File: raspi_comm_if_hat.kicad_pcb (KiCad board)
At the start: 2 copper layers, 65 x 56 mm, 64 parts, among them J1 B04B-XA, J2 Conn_02x20_Odd_Even, J3 B04B-XA, J4 Conn_01x02, J5 Conn_01x04, J6 B04B-XA, Q1 Q_NMOS_GSD, Q2 Q_NMOS_GSD, Q3 Q_NMOS_GSD, Q4 Q_NMOS_GSD, Q5 Q_NMOS_GSD, SW1 SW_DIP_x01, SW2 SW_DIP_x02, U1 MCP25625-x-SS, U2 74AHC1G04, U3 74AHC1G04, U4 TCK106AF, U5 TCK106AF, U6 CH213K, U7 CH213K, U8 TCK106AF, U9 TCK106AF, Y1 20MHz

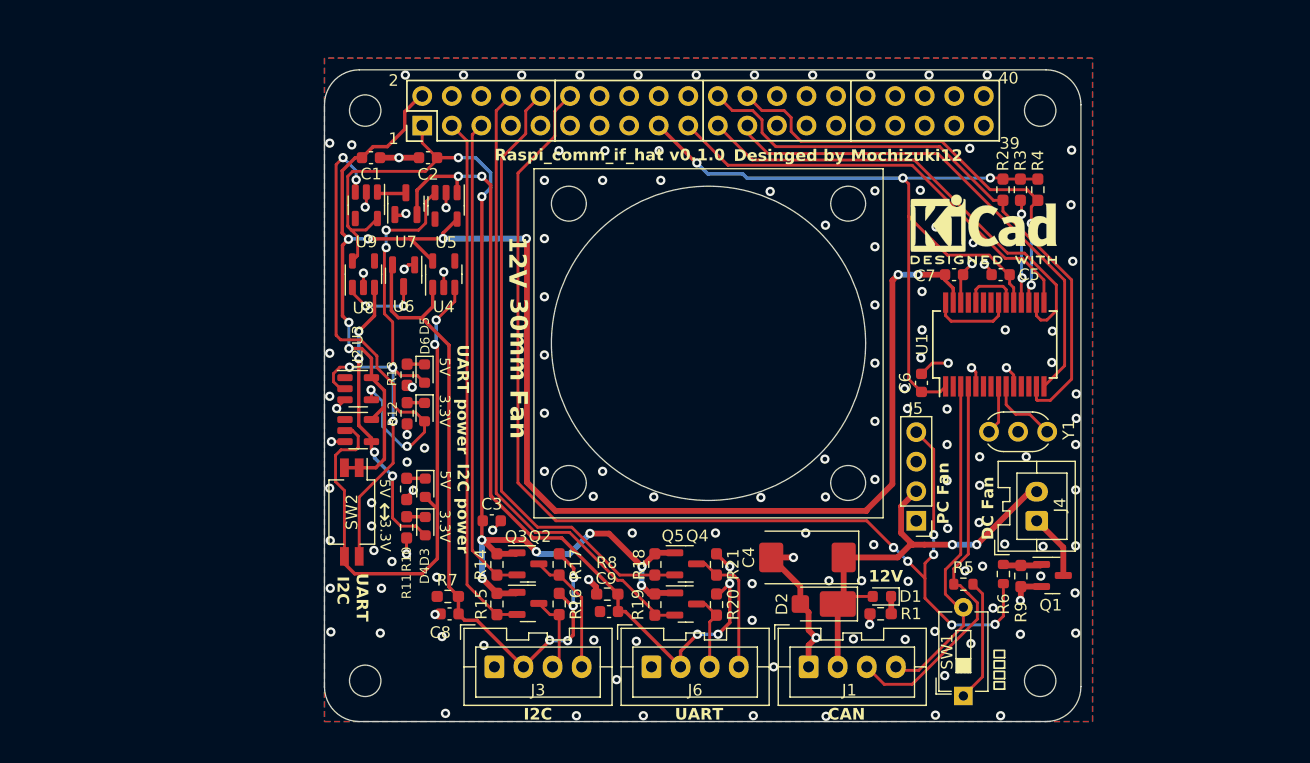
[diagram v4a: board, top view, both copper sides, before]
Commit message: Update of data for PCBA
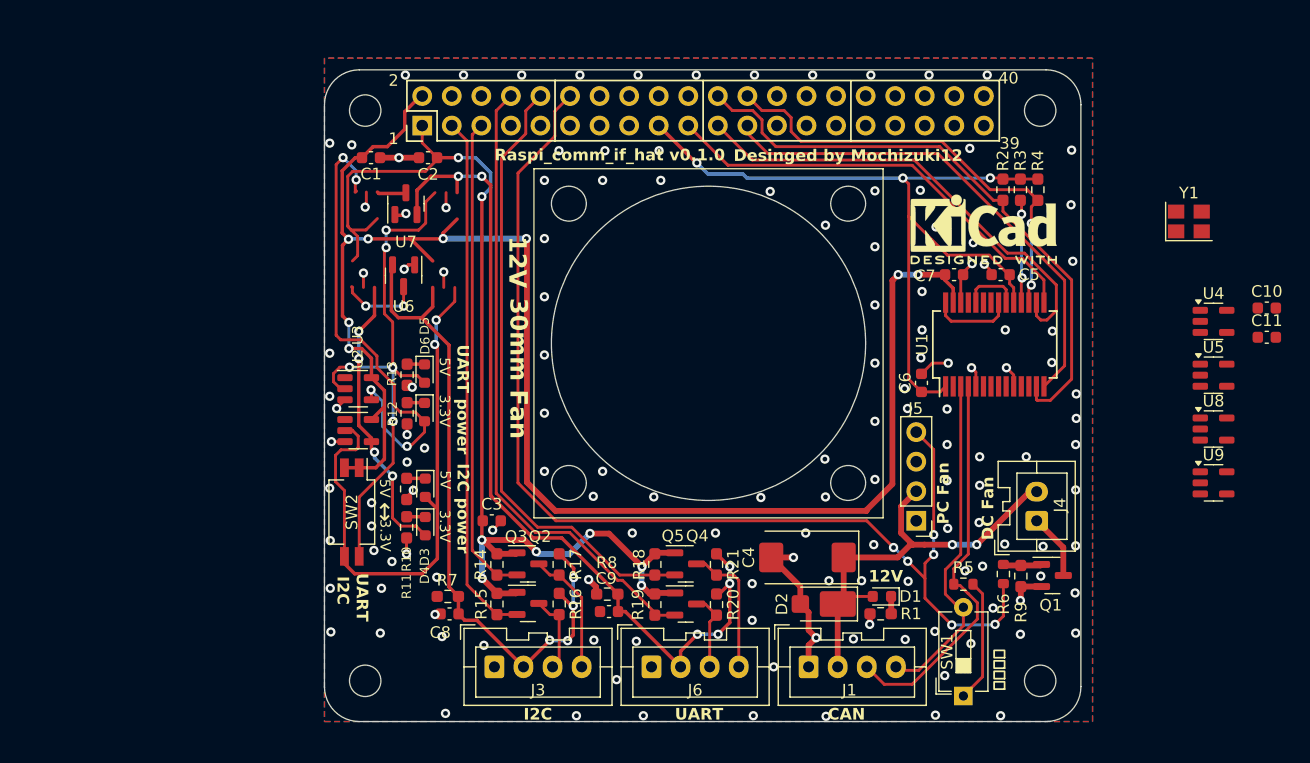
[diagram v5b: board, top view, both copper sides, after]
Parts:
- added C10: 9pF, Capacitor_SMD:C_0603_1608Metric, F.Cu at (181.0, 74.5)
- added C11: 9pF, Capacitor_SMD:C_0603_1608Metric, F.Cu at (181.0, 77.0)
- U4, U5, U8, U9: value TCK106AF -> AP2171W
- U6, U7: value CH213K -> AP2331
- Y1: value 20MHz -> 16MHz; footprint Crystal:Resonator_Murata_CSTLSxxxX-3Pin_W5.5mm_H3.0mm -> Crystal:Crystal_SMD_3225-4Pin_3.2x2.5mm
- moved U9 76.6 mm to (176.4, 89.5), turned to 0 degrees
- moved U8 74.2 mm to (176.4, 84.9), turned to 0 degrees
- moved U5 67.5 mm to (176.4, 80.2), turned to 0 degrees
- moved U4 66.3 mm to (176.4, 75.6), turned to 0 degrees
- moved Y1 21.8 mm to (174.3, 67.0), turned to 0 degrees
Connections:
- U4 pad 3: Net-(D3-A) -> unconnected-(U4-~{FLG}-Pad3)
- U4 pad 4: unconnected-(U4-NC-Pad4) -> Net-(D3-A)
- U5 pad 3: Net-(D5-A) -> unconnected-(U5-~{FLG}-Pad3)
- U5 pad 4: unconnected-(U5-NC-Pad4) -> Net-(D5-A)
- U8 pad 3: Net-(D4-A) -> unconnected-(U8-~{FLG}-Pad3)
- U8 pad 4: unconnected-(U8-NC-Pad4) -> Net-(D3-A)
- U9 pad 3: Net-(D6-A) -> unconnected-(U9-~{FLG}-Pad3)
- U9 pad 4: unconnected-(U9-NC-Pad4) -> Net-(D5-A)
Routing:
- net Net-(U1-OSC1): track 6.06 -> 0.00 mm
- net Net-(U1-OSC2): track 4.24 -> 0.00 mm

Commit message: Add LSCS
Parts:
- removed SW1: SW_DIP_x01, Button_Switch_THT:SW_DIP_SPSTx01_Slide_6.7x4.1mm_W7.62mm_P2.54mm_LowProfile
- added JP1: Jumper_2_Open, Connector_PinHeader_2.54mm:PinHeader_1x02_P2.54mm_Vertical, F.Cu at (154.7, 107.4)
- C10, C11: value 9pF -> 10pF; footprint Capacitor_SMD:C_0603_1608Metric -> Capacitor_SMD:C_0402_1005Metric
- C3, C5, C6, C7, C8, C9: footprint Capacitor_SMD:C_0603_1608Metric -> Capacitor_SMD:C_0402_1005Metric
- C4: value 100uF -> 10uF; footprint Capacitor_Tantalum_SMD:CP_EIA-7343-15_Kemet-W -> Capacitor_SMD:C_0603_1608Metric
- D2: footprint Diode_SMD:Vishay_SMPA -> Diode_SMD:D_SOD-123F
- R1, R10, R11, R12, R13, R14, R15, R16, R17, R18, R19, R2, R20, R21, R3, R4, R7, R8, R9: footprint Resistor_SMD:R_0603_1608Metric_Pad0.98x0.95mm_HandSolder -> Resistor_SMD:R_0402_1005Metric
- R6: footprint Resistor_SMD:R_0603_1608Metric -> Resistor_SMD:R_0402_1005Metric
- moved U5 74.3 mm to (103.5, 65.6), turned to -90 degrees
- moved U8 74.2 mm to (103.4, 71.6), turned to 90 degrees
- moved U9 70.2 mm to (110.4, 65.6), turned to -90 degrees
- moved U4 66.3 mm to (110.2, 71.6), turned to 90 degrees
- moved C11 26.1 mm to (156.2, 85.0), turned to 90 degrees
- moved Y1 23.8 mm to (158.8, 85.0), turned to 180 degrees
- moved C10 22.1 mm to (161.6, 85.0), turned to -90 degrees
- moved C4 3.38 mm to (144.5, 97.5)
- moved R6 1.59 mm to (159.8, 96.7), turned to -90 degrees
- moved R9 1.10 mm to (159.8, 98.6)
- moved R12 0.74 mm to (107.3, 79.5)
- moved C7 0.73 mm to (154.3, 72.3)
- moved R13 0.71 mm to (107.1, 82.8)
- moved R8 0.49 mm to (124.5, 99.5)
- moved R7 0.46 mm to (110.5, 99.7)
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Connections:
- U8 pad 4: Net-(D3-A) -> Net-(D4-A)
- U9 pad 4: Net-(D5-A) -> Net-(D6-A)
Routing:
- net Net-(D6-A): track 41.5 -> 32.7 mm
- net Net-(U1-OSC2): track 0.00 -> 7.55 mm
- net Net-(U1-OSC1): track 0.00 -> 5.79 mm
- net Net-(D4-A): track 25.0 -> 30.2 mm
- net Net-(U7-VI): track 2.50 -> 7.61 mm, vias 0 -> 2
- net UART_PWR: track 75.2 -> 78.6 mm
- net +3.3V: track 163.1 -> 166.0 mm, vias 11 -> 13
- net Net-(D3-A): track 48.8 -> 51.5 mm
- net FAN_PWM: track 99.5 -> 102.0 mm
- net Net-(D5-A): track 47.0 -> 44.7 mm
- net CS: track 38.5 -> 40.5 mm
- net Net-(J1-Pin_4): track 29.5 -> 31.4 mm
- net Net-(J1-Pin_3): track 34.0 -> 35.8 mm
- net +12V: track 37.4 -> 36.0 mm
- net +5V: track 142.5 -> 141.9 mm, vias 8 -> 6
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
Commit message: v0.2.0 release
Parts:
- removed J5: Conn_01x04, Connector_PinHeader_2.54mm:PinHeader_1x04_P2.54mm_Vertical
- removed U8, U9: AP2171W, Package_TO_SOT_SMD:SOT-23-5
- J1, J3, J6: footprint Connector_JST:JST_XA_B04B-XASK-1_1x04_P2.50mm_Vertical -> Connector_JST:JST_XA_S04B-XASK-1_1x04_P2.50mm_Horizontal
- U4, U5: value AP2171W -> XC8110
- U6, U7: value AP2331 -> XC8110; footprint Package_TO_SOT_SMD:SOT-23 -> Package_TO_SOT_SMD:SOT-23-5
- moved U3 16.3 mm to (107.0, 65.6), turned to -90 degrees
- moved U2 13.5 mm to (107.0, 72.1), turned to 90 degrees
- moved D4 10.9 mm to (104.0, 83.4)
- moved D3 10.9 mm to (104.0, 80.1)
- moved R10 10.9 mm to (102.4, 80.2)
- moved R11 10.9 mm to (102.4, 83.5)
- moved U6 6.88 mm to (103.6, 65.6), turned to 90 degrees
- moved U5 6.46 mm to (103.6, 72.1)
- moved R19 6.41 mm to (130.6, 93.9), turned to 180 degrees
- moved R20 6.29 mm to (128.0, 97.3), turned to 90 degrees
- moved R16 6.26 mm to (114.4, 97.5), turned to 90 degrees
- moved R18 6.26 mm to (134.1, 93.9), turned to 180 degrees
- moved R15 6.22 mm to (117.2, 94.1), turned to 180 degrees
- moved R14 6.11 mm to (120.5, 94.1), turned to 180 degrees
- moved Q4 3.67 mm to (130.2, 96.3), turned to -90 degrees
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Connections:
- U4 pad 1: I2C_PWR -> +5V
- U4 pad 3: unconnected-(U4-~{FLG}-Pad3) -> Net-(D3-A)
- U4 pad 4: Net-(D3-A) -> unconnected-(U4-NC-Pad4)
- U4 pad 5: +5V -> I2C_PWR
- U5 pad 1: UART_PWR -> +3.3V
- U5 pad 3: unconnected-(U5-~{FLG}-Pad3) -> Net-(D4-A)
- U5 pad 4: Net-(D5-A) -> unconnected-(U5-NC-Pad4)
- U5 pad 5: +5V -> I2C_PWR
- U6 pad 1: GND -> +5V
- U6 pad 2: I2C_PWR -> GND
- U6 pad 3: Net-(U6-VI) -> Net-(D5-A)
- U7 pad 1: GND -> +3.3V
- U7 pad 2: UART_PWR -> GND
- U7 pad 3: Net-(U7-VI) -> Net-(D6-A)
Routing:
- net +3.3V: track 166.0 -> 152.5 mm, vias 13 -> 14
- net FAN_PWM: track 102.0 -> 88.6 mm, vias 6 -> 4
- net Net-(D3-A): track 51.5 -> 41.9 mm
- net UART_PWR: track 78.6 -> 70.3 mm, vias 6 -> 3
- net Net-(U7-VI): track 7.61 -> 0.00 mm, vias 2 -> 0
- net Net-(U6-VI): track 6.81 -> 0.00 mm, vias 2 -> 0
- net +12V: track 36.0 -> 29.5 mm
- net Net-(D4-A): track 30.2 -> 23.7 mm, vias 4 -> 0
- net I2C_PWR: track 58.6 -> 52.9 mm, vias 4 -> 1
- net Net-(D5-A): track 44.7 -> 39.2 mm, vias 5 -> 4
- net Net-(D6-A): track 32.7 -> 28.0 mm, vias 4 -> 2
- net GND: track 47.1 -> 42.9 mm, vias 150 -> 151
- net SDA: track 45.1 -> 41.4 mm
- net RX_conn: track 11.7 -> 8.11 mm
- net SDL_conn: track 11.1 -> 7.98 mm
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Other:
- board text added: "ON"
- board text added: "Raspi_comm_if_hat v0.2.0"
- board text removed: "PC Fan"
- board text removed: "Raspi_comm_if_hat v0.1.0"
